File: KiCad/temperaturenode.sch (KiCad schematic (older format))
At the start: 10 parts

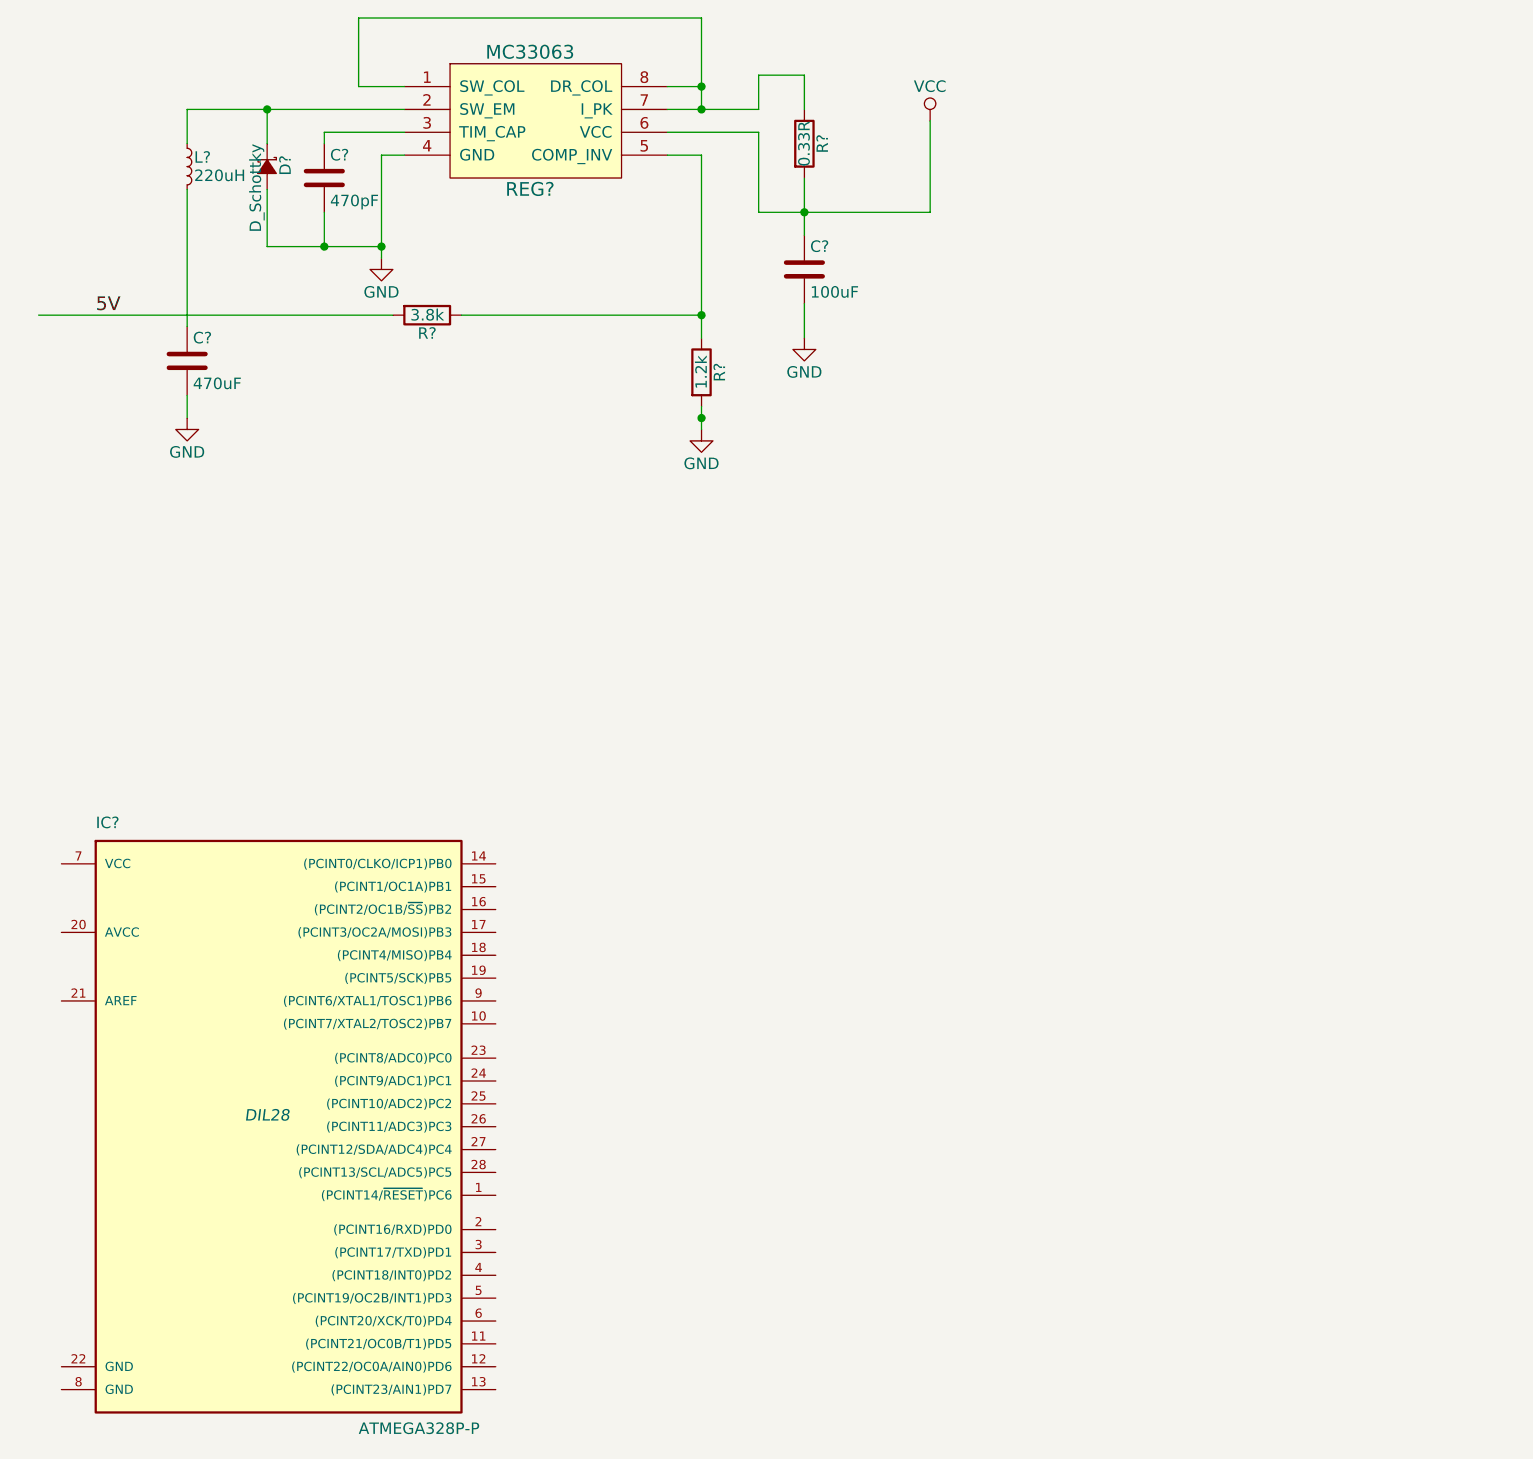
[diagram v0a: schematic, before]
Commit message: Made a standalone pdu to test
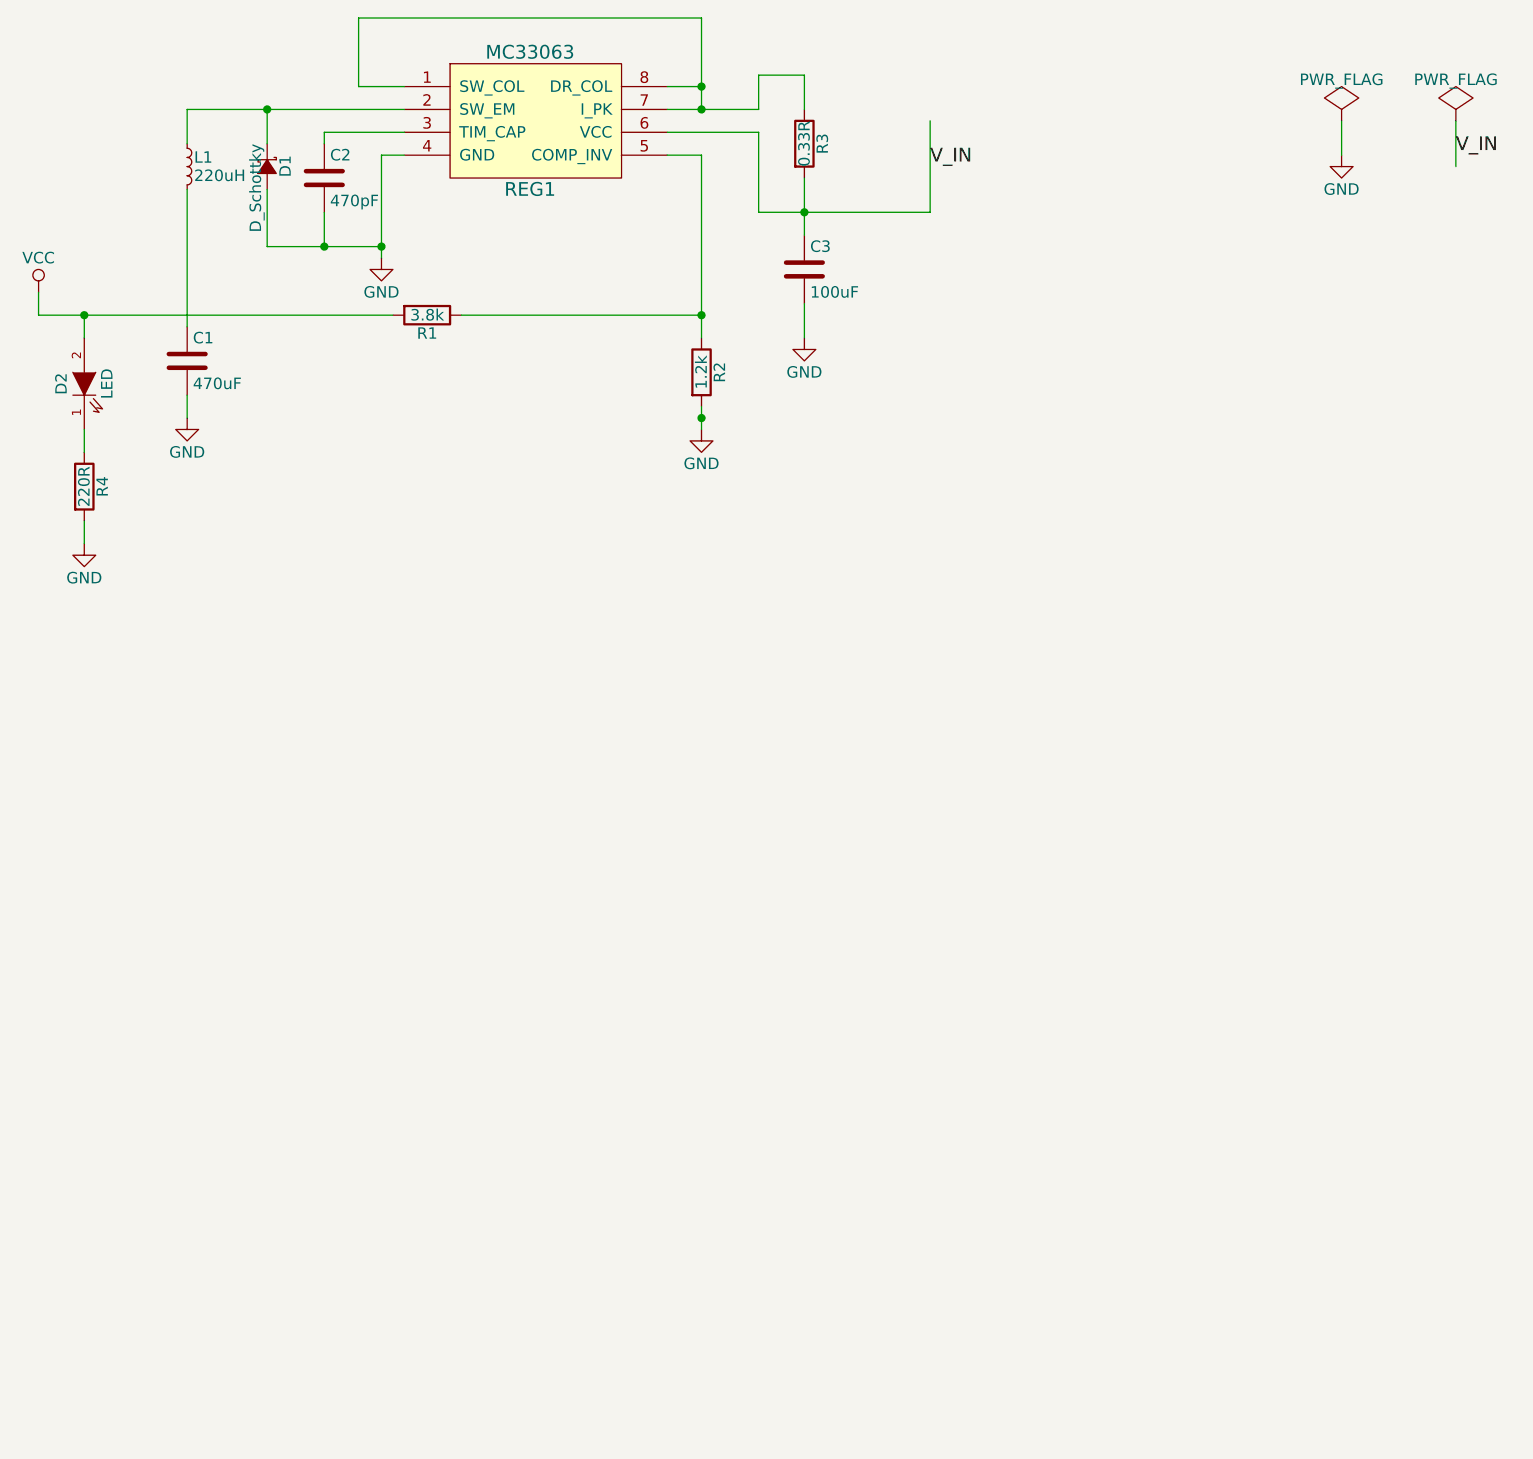
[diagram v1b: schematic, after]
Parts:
- removed IC?: ATMEGA328P-P, DIL28, symbol ATMEGA328P-P
- added D2: LED, LEDs:LED-3MM, symbol LED
- added R4: 220R, Resistors_ThroughHole:Resistor_Vertical_RM5mm, symbol R
- C1, C2, C3: renamed from C?; footprint (none) -> Capacitors_ThroughHole:C_Disc_D6_P5
- D1: renamed from D?; footprint (none) -> Diodes_ThroughHole:Diode_DO-41_SOD81_Horizontal_RM10
- L1: renamed from L?; footprint (none) -> Choke_Toroid_ThroughHole:Choke_Toroid_horizontal_Diameter9mm_Amidon-T30
- R1, R2, R3: renamed from R?; footprint (none) -> Resistors_ThroughHole:Resistor_Vertical_RM5mm
- REG1: renamed from REG?; footprint (none) -> Housings_DIP:DIP-8_W7.62mm
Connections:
- net labels added: V_IN
- net labels removed: 5V
- wire segments 32 -> 38
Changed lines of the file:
@@
 $EndDescr
 $Comp
-L ATMEGA328P-P IC?
-U 1 1 57EDE05B
-P 2550 6150
-F 0 "IC?" H 1800 7400 50  0000 L BNN
-F 1 "ATMEGA328P-P" H 2950 4750 50  0000 L BNN
-F 2 "DIL28" H 2550 6150 50  0000 C CIN
-F 3 "" H 2550 6150 50  0000 C CNN
-	1    2550 6150
-	1    0    0    -1
-$EndComp
-$Comp
-L MC33063 REG?
+L MC33063 REG1
 U 1 1 57EDE6C7
 P 3750 1850
-F 0 "REG?" H 3700 1600 60  0000 C CNN
+F 0 "REG1" H 3700 1600 60  0000 C CNN
 F 1 "MC33063" H 3700 2200 60  0000 C CNN
-F 2 "" H 3650 1700 60  0001 C CNN
+F 2 "Housings_DIP:DIP-8_W7.62mm" H 3650 1700 60  0001 C CNN
 F 3 "" H 3650 1700 60  0001 C CNN
 	1    3750 1850
@@
 $EndComp
 $Comp
-L R R?
+L R R3
 U 1 1 57EDE8F2
 P 4900 1900
-F 0 "R?" V 4980 1900 50  0000 C CNN
+F 0 "R3" V 4980 1900 50  0000 C CNN
 F 1 "0.33R" V 4900 1900 50  0000 C CNN
-F 2 "" V 4830 1900 50  0000 C CNN
+F 2 "Resistors_ThroughHole:Resistor_Vertical_RM5mm" V 4830 1900 50  0001 C CNN
 F 3 "" H 4900 1900 50  0000 C CNN
 	1    4900 1900
@@
 $EndComp
 $Comp
-L R R?
+L R R2
 U 1 1 57EDE950
 P 4450 2900
-F 0 "R?" V 4530 2900 50  0000 C CNN
+F 0 "R2" V 4530 2900 50  0000 C CNN
 F 1 "1.2k" V 4450 2900 50  0000 C CNN
-F 2 "" V 4380 2900 50  0000 C CNN
+F 2 "Resistors_ThroughHole:Resistor_Vertical_RM5mm" V 4380 2900 50  0001 C CNN
 F 3 "" H 4450 2900 50  0000 C CNN
 	1    4450 2900
@@
 $EndComp
 $Comp
-L R R?
+L R R1
 U 1 1 57EDE97A
 P 3250 2650
-F 0 "R?" V 3330 2650 50  0000 C CNN
+F 0 "R1" V 3330 2650 50  0000 C CNN
 F 1 "3.8k" V 3250 2650 50  0000 C CNN
-F 2 "" V 3180 2650 50  0000 C CNN
+F 2 "Resistors_ThroughHole:Resistor_Vertical_RM5mm" V 3180 2650 50  0001 C CNN
 F 3 "" H 3250 2650 50  0000 C CNN
 	1    3250 2650
@@
 $EndComp
 $Comp
-L L_Small L?
+L L_Small L1
 U 1 1 57EDEC57
 P 2200 2000
-F 0 "L?" H 2230 2040 50  0000 L CNN
+F 0 "L1" H 2230 2040 50  0000 L CNN
 F 1 "220uH" H 2230 1960 50  0000 L CNN
-F 2 "" H 2200 2000 50  0000 C CNN
+F 2 "Choke_Toroid_ThroughHole:Choke_Toroid_horizontal_Diameter9mm_Amidon-T30" H 2200 2000 50  0001 C CNN
 F 3 "" H 2200 2000 50  0000 C CNN
 	1    2200 2000
@@
 $EndComp
 $Comp
-L C C?
+L C C1
 U 1 1 57EDED98
 P 2200 2850
-F 0 "C?" H 2225 2950 50  0000 L CNN
+F 0 "C1" H 2225 2950 50  0000 L CNN
 F 1 "470uF" H 2225 2750 50  0000 L CNN
-F 2 "" H 2238 2700 50  0000 C CNN
+F 2 "Capacitors_ThroughHole:C_Disc_D6_P5" H 2238 2700 50  0001 C CNN
 F 3 "" H 2200 2850 50  0000 C CNN
 	1    2200 2850
@@
 $EndComp
 $Comp
-L C C?
+L C C3
 U 1 1 57EDEDE4
 P 4900 2450
-F 0 "C?" H 4925 2550 50  0000 L CNN
+F 0 "C3" H 4925 2550 50  0000 L CNN
 F 1 "100uF" H 4925 2350 50  0000 L CNN
-F 2 "" H 4938 2300 50  0000 C CNN
+F 2 "Capacitors_ThroughHole:C_Disc_D6_P5" H 4938 2300 50  0001 C CNN
 F 3 "" H 4900 2450 50  0000 C CNN
 	1    4900 2450
@@
 $EndComp
 $Comp
-L C C?
+L C C2
 U 1 1 57EDEE1C
 P 2800 2050
-F 0 "C?" H 2825 2150 50  0000 L CNN
+F 0 "C2" H 2825 2150 50  0000 L CNN
 F 1 "470pF" H 2825 1950 50  0000 L CNN
-F 2 "" H 2838 1900 50  0000 C CNN
+F 2 "Capacitors_ThroughHole:C_Disc_D6_P5" H 2838 1900 50  0001 C CNN
 F 3 "" H 2800 2050 50  0000 C CNN
 	1    2800 2050
@@
 $EndComp
 $Comp
-L GND #PWR?
+L GND #PWR01
 U 1 1 57EDF7CC
 P 3050 2400
-F 0 "#PWR?" H 3050 2150 50  0001 C CNN
+F 0 "#PWR01" H 3050 2150 50  0001 C CNN
 F 1 "GND" H 3050 2250 50  0000 C CNN
 F 2 "" H 3050 2400 50  0000 C CNN
@@
 $EndComp
 $Comp
-L GND #PWR?
+L GND #PWR02
 U 1 1 57EDF8BC
 P 4450 3150
-F 0 "#PWR?" H 4450 2900 50  0001 C CNN
+F 0 "#PWR02" H 4450 2900 50  0001 C CNN
 F 1 "GND" H 4450 3000 50  0000 C CNN
 F 2 "" H 4450 3150 50  0000 C CNN
@@
 $EndComp
 $Comp
-L GND #PWR?
+L GND #PWR03
 U 1 1 57EDFC01
 P 4900 2750
-F 0 "#PWR?" H 4900 2500 50  0001 C CNN
+F 0 "#PWR03" H 4900 2500 50  0001 C CNN
 F 1 "GND" H 4900 2600 50  0000 C CNN
 F 2 "" H 4900 2750 50  0000 C CNN
@@
 $EndComp
 $Comp
-L D_Schottky_Small D?
+L D_Schottky_Small D1
 U 1 1 57EE096B
 P 2550 2000
-F 0 "D?" H 2500 2080 50  0000 L CNN
+F 0 "D1" H 2500 2080 50  0000 L CNN
 F 1 "D_Schottky" H 2450 1950 50  0000 L CNN
-F 2 "" V 2550 2000 50  0000 C CNN
+F 2 "Diodes_ThroughHole:Diode_DO-41_SOD81_Horizontal_RM10" V 2550 2000 50  0001 C CNN
 F 3 "" V 2550 2000 50  0000 C CNN
 	1    2550 2000
@@
 $EndComp
 $Comp
-L GND #PWR?
+L GND #PWR04
 U 1 1 57EE0EEE
 P 2200 3100
-F 0 "#PWR?" H 2200 2850 50  0001 C CNN
+F 0 "#PWR04" H 2200 2850 50  0001 C CNN
 F 1 "GND" H 2200 2950 50  0000 C CNN
 F 2 "" H 2200 3100 50  0000 C CNN
@@
 Wire Wire Line
 	1550 2650 3100 2650
-Text Label 1800 2650 0    60   ~ 0
-5V
-$Comp
-L VCC #PWR?
-U 1 1 57EE076E
-P 5450 1800
-F 0 "#PWR?" H 5450 1650 50  0001 C CNN
-F 1 "VCC" H 5450 1950 50  0000 C CNN
-F 2 "" H 5450 1800 50  0000 C CNN
-F 3 "" H 5450 1800 50  0000 C CNN
-	1    5450 1800
-	1    0    0    -1
-$EndComp
+$Comp
+L VCC #PWR05
+U 1 1 57EE1D65
+P 1550 2550
+F 0 "#PWR05" H 1550 2400 50  0001 C CNN
+F 1 "VCC" H 1550 2700 50  0000 C CNN
+F 2 "" H 1550 2550 50  0000 C CNN
+F 3 "" H 1550 2550 50  0000 C CNN
+	1    1550 2550
+	1    0    0    -1
+$EndComp
+Wire Wire Line
+	1550 2650 1550 2550
+Text Label 5450 2000 0    60   ~ 0
+V_IN
+$Comp
+L PWR_FLAG #FLG06
+U 1 1 57EE1E8E
+P 7250 1800
+F 0 "#FLG06" H 7250 1895 50  0001 C CNN
+F 1 "PWR_FLAG" H 7250 1980 50  0000 C CNN
+F 2 "" H 7250 1800 50  0000 C CNN
+F 3 "" H 7250 1800 50  0000 C CNN
+	1    7250 1800
+	1    0    0    -1
+$EndComp
+$Comp
+L PWR_FLAG #FLG07
+U 1 1 57EE1EBB
+P 7750 1800
+F 0 "#FLG07" H 7750 1895 50  0001 C CNN
+F 1 "PWR_FLAG" H 7750 1980 50  0000 C CNN
+F 2 "" H 7750 1800 50  0000 C CNN
+F 3 "" H 7750 1800 50  0000 C CNN
+	1    7750 1800
+	1    0    0    -1
+$EndComp
+$Comp
+L GND #PWR08
+U 1 1 57EE1EE1
+P 7250 1950
+F 0 "#PWR08" H 7250 1700 50  0001 C CNN
+F 1 "GND" H 7250 1800 50  0000 C CNN
+F 2 "" H 7250 1950 50  0000 C CNN
+F 3 "" H 7250 1950 50  0000 C CNN
+	1    7250 1950
+	1    0    0    -1
+$EndComp
+Wire Wire Line
+	7250 1800 7250 1950
+Wire Wire Line
+	7750 1800 7750 2000
+Text Label 7750 1950 0    60   ~ 0
+V_IN
+$Comp
+L LED D2
+U 1 1 57EE252B
+P 1750 2950
+F 0 "D2" H 1750 3050 50  0000 C CNN
+F 1 "LED" H 1750 2850 50  0000 C CNN
+F 2 "LEDs:LED-3MM" H 1750 2950 50  0001 C CNN
+F 3 "" H 1750 2950 50  0000 C CNN
+	1    1750 2950
+	0    -1   -1   0
+$EndComp
+$Comp
+L R R4
+U 1 1 57EE25E2
+P 1750 3400
+F 0 "R4" V 1830 3400 50  0000 C CNN
+F 1 "220R" V 1750 3400 50  0000 C CNN
+F 2 "Resistors_ThroughHole:Resistor_Vertical_RM5mm" V 1680 3400 50  0001 C CNN
+F 3 "" H 1750 3400 50  0000 C CNN
+	1    1750 3400
+	1    0    0    -1
+$EndComp
+$Comp
+L GND #PWR09
+U 1 1 57EE2803
+P 1750 3650
+F 0 "#PWR09" H 1750 3400 50  0001 C CNN
+F 1 "GND" H 1750 3500 50  0000 C CNN
+F 2 "" H 1750 3650 50  0000 C CNN
+F 3 "" H 1750 3650 50  0000 C CNN
+	1    1750 3650
+	1    0    0    -1
+$EndComp
+Wire Wire Line
+	1750 3550 1750 3650
+Wire Wire Line
+	1750 3250 1750 3150
+Wire Wire Line
+	1750 2750 1750 2650
+Connection ~ 1750 2650
 $EndSCHEMATC
